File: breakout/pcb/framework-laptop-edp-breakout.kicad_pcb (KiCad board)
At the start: 2 copper layers, 29 x 46 mm, 6 parts, among them J1 20879-040E-01, J2 Conn_01x40

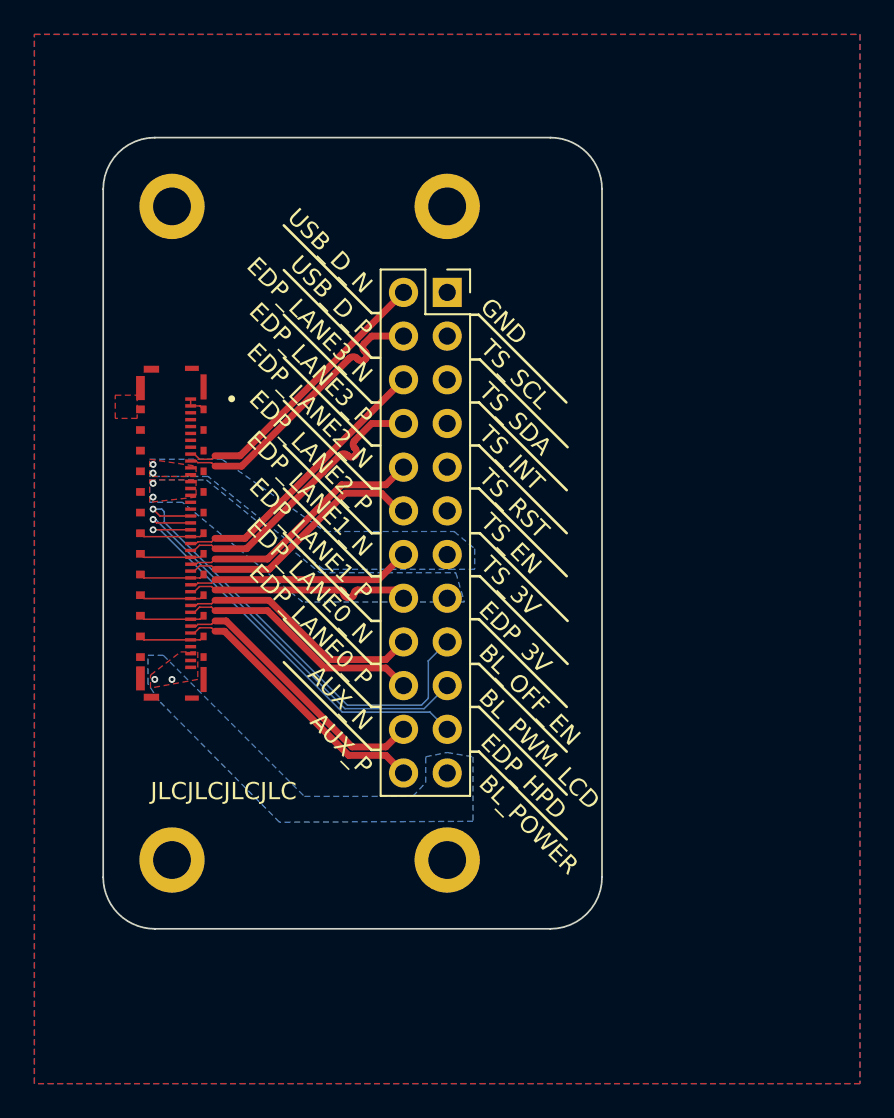
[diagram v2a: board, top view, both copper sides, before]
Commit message: finish up routing on breakout
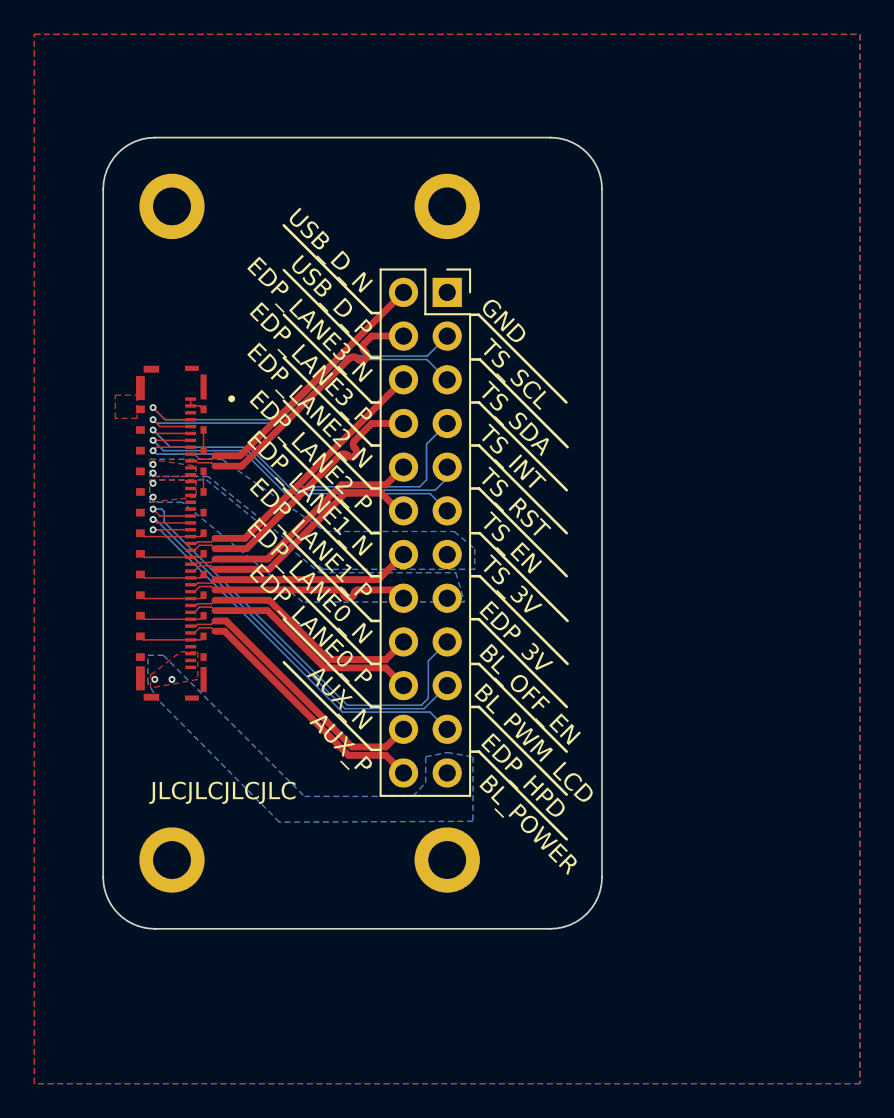
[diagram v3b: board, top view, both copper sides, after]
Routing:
- net TS_INT_N: track 0.00 -> 23.5 mm, vias 0 -> 1
- net TS_SCL: track 0.00 -> 21.9 mm, vias 0 -> 1
- net TS_SDA: track 0.00 -> 21.6 mm, vias 0 -> 1
- net TS_RST: track 0.00 -> 21.4 mm, vias 0 -> 1
- net TS_EN: track 0.00 -> 20.8 mm, vias 0 -> 1
- net GND: track 24.2 -> 26.6 mm
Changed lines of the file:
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@@
     (effects (font (size 1 1) (thickness 0.125)) (justify right mirror))
   )
-  (gr_text "BL_PWM_LCD" (at 175.9908 84.8 45) (layer "B.SilkS")
+  (gr_text "BL_PWM_LCD" (at 175.7 85.1 45) (layer "B.SilkS")
     (effects (font (size 1 1) (thickness 0.125)) (justify right mirror))
   )
@@
     (effects (font (size 1 1) (thickness 0.125)) (justify right))
   )
-  (gr_text "BL_PWM_LCD" (at 176.1 85.3 -45) (layer "F.SilkS")
+  (gr_text "BL_PWM_LCD" (at 175.8 85 -45) (layer "F.SilkS")
     (effects (font (size 1 1) (thickness 0.125)) (justify left))
   )
@@
   (segment (start 172.66 86.2) (end 168.05 86.2) (width 0.09) (layer "B.Cu") (net 12))
   (segment (start 157.05 75.2) (end 156.9 75.2) (width 0.09) (layer "B.Cu") (net 12))
-  (segment (start 159.0825 75) (end 159.4 75) (width 0.09) (layer "F.Cu") (net 13))
   (segment (start 157.3 75) (end 156.9 74.6) (width 0.09) (layer "F.Cu") (net 13))
   (segment (start 159.0825 75) (end 157.3 75) (width 0.09) (layer "F.Cu") (net 13))
@@
   (segment (start 160.3 71.7) (end 160.5 71.5) (width 0.09) (layer "F.Cu") (net 15))
   (segment (start 159.3 71.4) (end 159.6 71.7) (width 0.09) (layer "F.Cu") (net 15))
+  (segment (start 157.1 71) (end 159.0825 71) (width 0.09) (layer "F.Cu") (net 16))
+  (segment (start 156.9 71.2) (end 157.1 71) (width 0.09) (layer "F.Cu") (net 16))
+  (via (at 156.9 71.2) (size 0.4) (drill 0.2) (layers "F.Cu" "B.Cu") (net 16))
+  (segment (start 162.3 71.4) (end 164.6 73.7) (width 0.09) (layer "B.Cu") (net 16))
+  (segment (start 164.6 73.7) (end 173 73.7) (width 0.09) (layer "B.Cu") (net 16))
+  (segment (start 156.9 71.2) (end 157.1 71.4) (width 0.09) (layer "B.Cu") (net 16))
+  (segment (start 173 73.7) (end 174 74.7) (width 0.09) (layer "B.Cu") (net 16))
+  (segment (start 157.1 71.4) (end 162.3 71.4) (width 0.09) (layer "B.Cu") (net 16))
+  (segment (start 159.0825 70.6) (end 156.9 70.6) (width 0.09) (layer "F.Cu") (net 17))
+  (via (at 156.9 70.6) (size 0.4) (drill 0.2) (layers "F.Cu" "B.Cu") (net 17))
+  (segment (start 173.3 73.5) (end 174 72.8) (width 0.09) (layer "B.Cu") (net 17))
+  (segment (start 156.9 70.6) (end 157.5 71.2) (width 0.09) (layer "B.Cu") (net 17))
+  (segment (start 157.5 71.2) (end 162.4 71.2) (width 0.09) (layer "B.Cu") (net 17))
+  (segment (start 174 72.8) (end 174 72.16) (width 0.09) (layer "B.Cu") (net 17))
+  (segment (start 162.4 71.2) (end 164.7 73.5) (width 0.09) (layer "B.Cu") (net 17))
+  (segment (start 164.7 73.5) (end 173.3 73.5) (width 0.09) (layer "B.Cu") (net 17))
+  (segment (start 159.0825 70.2) (end 157.1 70.2) (width 0.09) (layer "F.Cu") (net 18))
+  (segment (start 157.1 70.2) (end 156.9 70) (width 0.09) (layer "F.Cu") (net 18))
+  (via (at 156.9 70) (size 0.4) (drill 0.2) (layers "F.Cu" "B.Cu") (net 18))
+  (segment (start 157.9 71) (end 162.5 71) (width 0.09) (layer "B.Cu") (net 18))
+  (segment (start 172.8 72.9) (end 172.8 70.82) (width 0.09) (layer "B.Cu") (net 18))
+  (segment (start 172.4 73.3) (end 172.8 72.9) (width 0.09) (layer "B.Cu") (net 18))
+  (segment (start 162.5 71) (end 164.8 73.3) (width 0.09) (layer "B.Cu") (net 18))
+  (segment (start 172.8 70.82) (end 174 69.62) (width 0.09) (layer "B.Cu") (net 18))
+  (segment (start 156.9 70) (end 157.9 71) (width 0.09) (layer "B.Cu") (net 18))
+  (segment (start 164.8 73.3) (end 172.4 73.3) (width 0.09) (layer "B.Cu") (net 18))
+  (segment (start 156.9 69.4) (end 157.3 69.8) (width 0.09) (layer "F.Cu") (net 19))
+  (segment (start 157.3 69.8) (end 159.0825 69.8) (width 0.09) (layer "F.Cu") (net 19))
+  (via (at 156.9 69.4) (size 0.4) (drill 0.2) (layers "F.Cu" "B.Cu") (net 19))
+  (segment (start 156.9 69.4) (end 157.1 69.6) (width 0.09) (layer "B.Cu") (net 19))
+  (segment (start 164.1 69.6) (end 167.8 65.9) (width 0.09) (layer "B.Cu") (net 19))
+  (segment (start 172.82 65.9) (end 174 67.08) (width 0.09) (layer "B.Cu") (net 19))
+  (segment (start 167.8 65.9) (end 172.82 65.9) (width 0.09) (layer "B.Cu") (net 19))
+  (segment (start 157.1 69.6) (end 164.1 69.6) (width 0.09) (layer "B.Cu") (net 19))
+  (segment (start 157.6 69.4) (end 159.0825 69.4) (width 0.09) (layer "F.Cu") (net 20))
+  (segment (start 156.9 68.7) (end 157.6 69.4) (width 0.09) (layer "F.Cu") (net 20))
+  (via (at 156.9 68.7) (size 0.4) (drill 0.2) (layers "F.Cu" "B.Cu") (net 20))
+  (segment (start 164 69.4) (end 167.7 65.7) (width 0.09) (layer "B.Cu") (net 20))
+  (segment (start 156.9 68.7) (end 157.6 69.4) (width 0.09) (layer "B.Cu") (net 20))
+  (segment (start 167.7 65.7) (end 172.84 65.7) (width 0.09) (layer "B.Cu") (net 20))
+  (segment (start 157.6 69.4) (end 164 69.4) (width 0.09) (layer "B.Cu") (net 20))
+  (segment (start 172.84 65.7) (end 174 64.54) (width 0.09) (layer "B.Cu") (net 20))
   (segment (start 159.0825 78.6) (end 159.6325 78.6) (width 0.09) (layer "F.Cu") (net 21))
   (segment (start 159.0825 76.2) (end 159.6325 76.2) (width 0.09) (layer "F.Cu") (net 21))
   (segment (start 156.3675 76.2) (end 156.1675 76) (width 0.09) (layer "F.Cu") (net 21))
+  (segment (start 159.8325 71.2) (end 159.8325 70) (width 0.09) (layer "F.Cu") (net 21))
   (segment (start 156.3675 81) (end 156.1675 80.8) (width 0.09) (layer "F.Cu") (net 21))
   (segment (start 156.3675 79.8) (end 156.1675 79.6) (width 0.09) (layer "F.Cu") (net 21))
@@
   (segment (start 159.0825 68.6) (end 159.6325 68.6) (width 0.09) (layer "F.Cu") (net 21))
   (segment (start 156.3675 82.2) (end 156.1675 82) (width 0.09) (layer "F.Cu") (net 21))
+  (segment (start 159.8325 72.4) (end 159.8325 73.6) (width 0.09) (layer "F.Cu") (net 21))
   (segment (start 159.6325 68.6) (end 159.8325 68.8) (width 0.09) (layer "F.Cu") (net 21))
   (segment (start 159.0825 82.2) (end 156.3675 82.2) (width 0.09) (layer "F.Cu") (net 21))
